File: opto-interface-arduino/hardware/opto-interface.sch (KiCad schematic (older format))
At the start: 24 parts, among them P1 CONN_02X06, P2 CONN_01X06, U1 max889, U2 LM7805, U3 LM7905

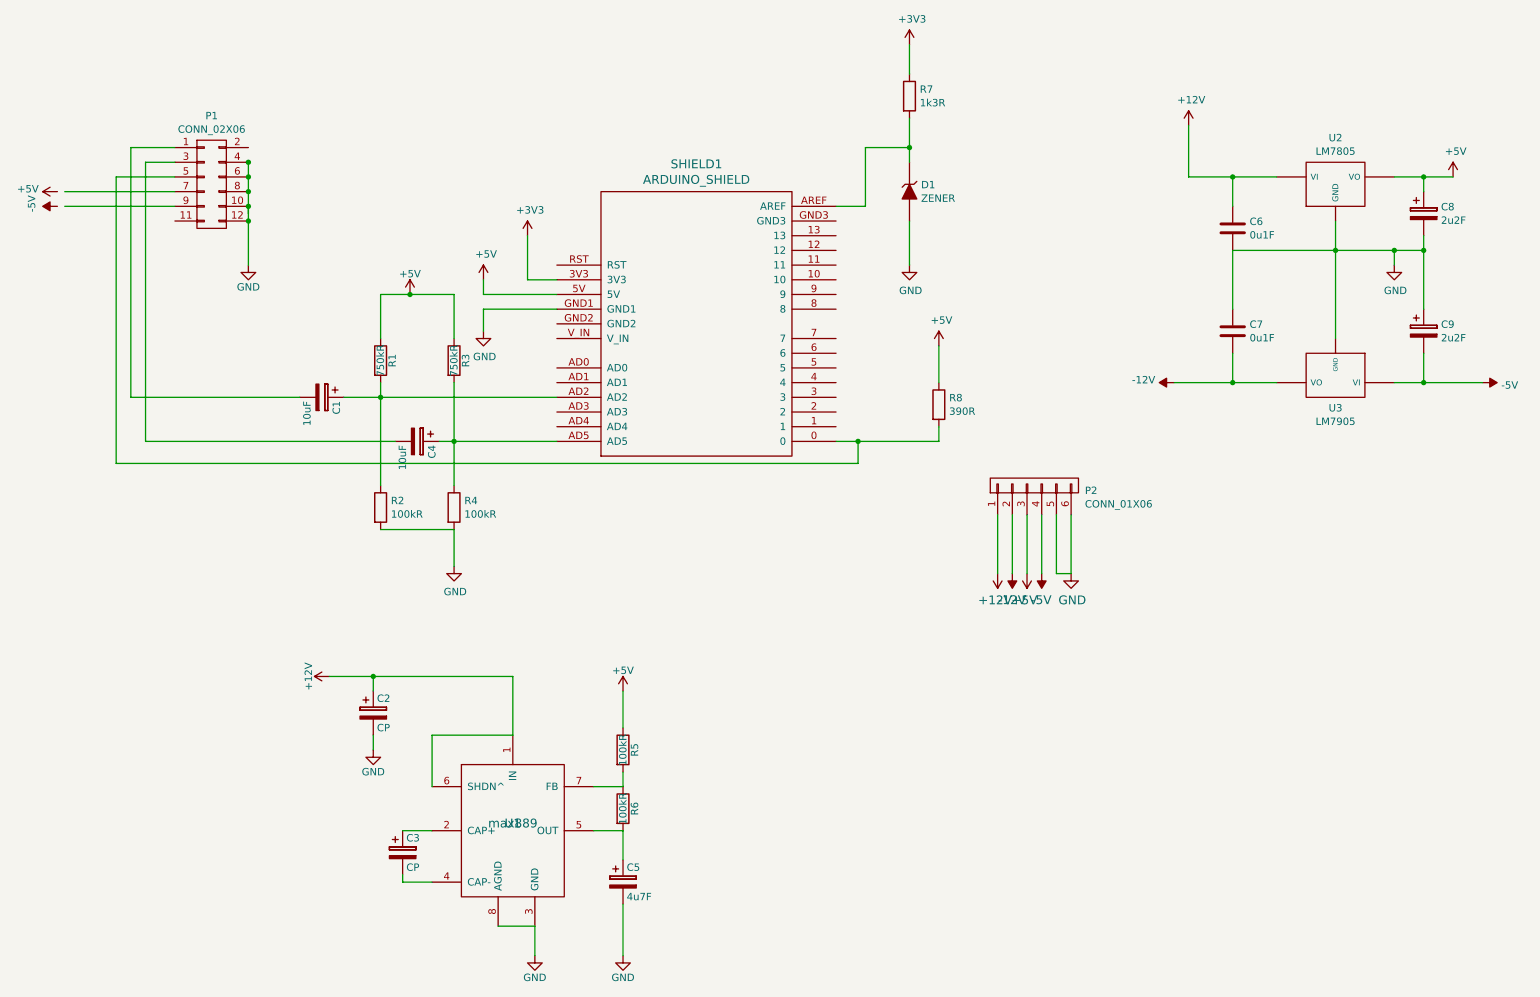
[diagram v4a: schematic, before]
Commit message: Modify layout to ahem follow the datasheet guidance on MAX889. Update analogue input schematic for simulation to accomodate steeper low-pass roll-off.
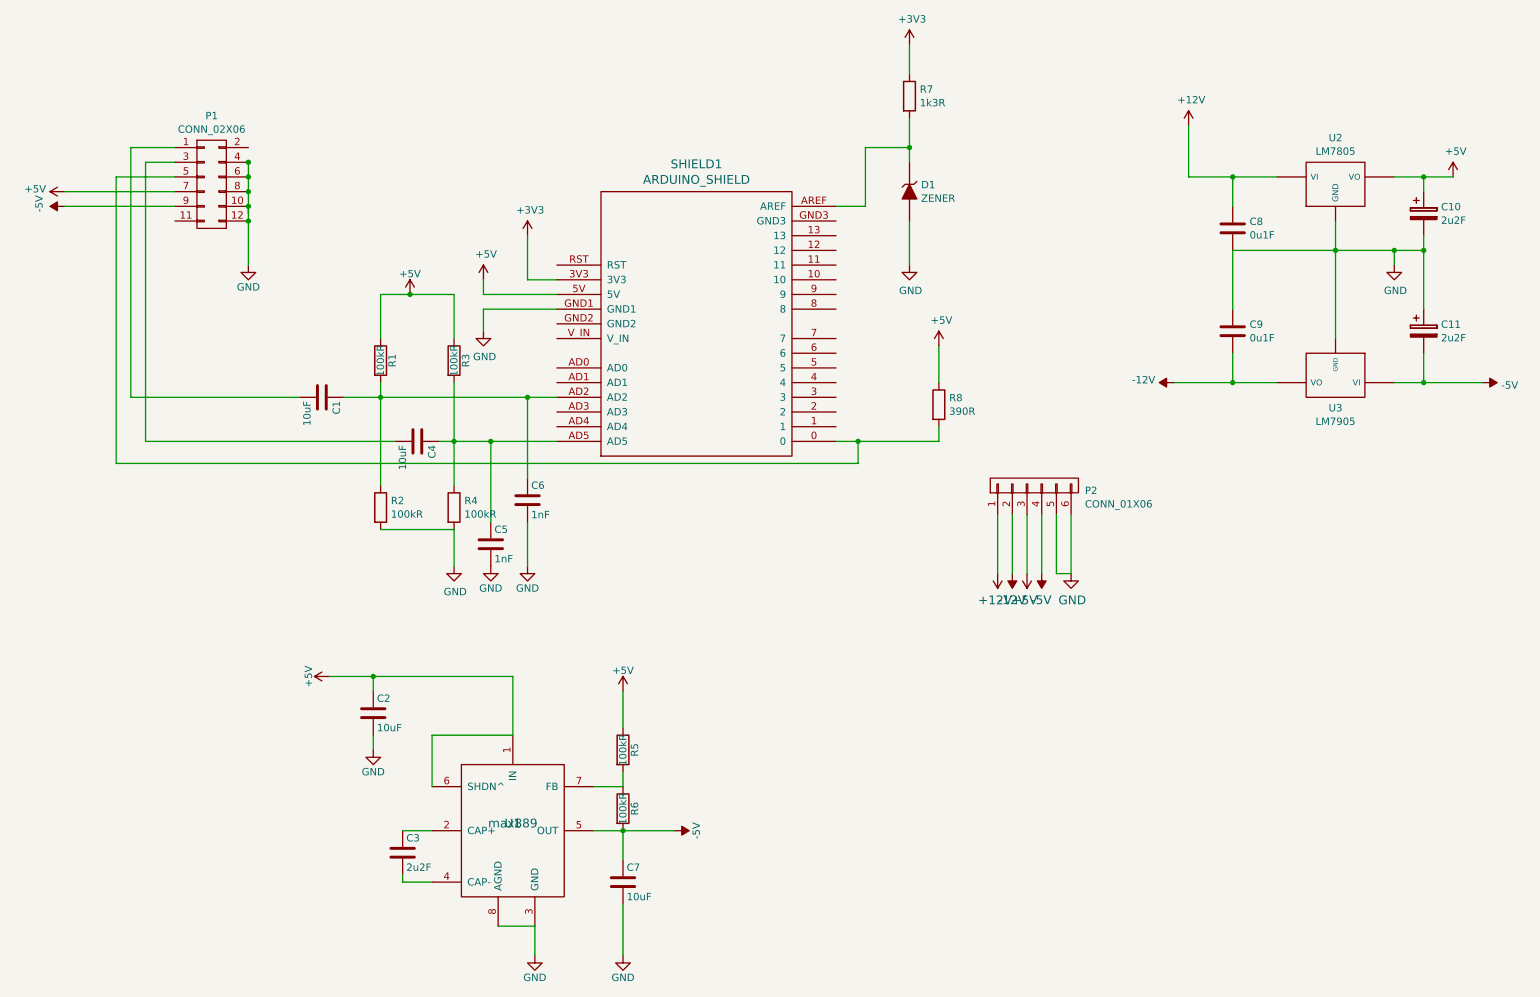
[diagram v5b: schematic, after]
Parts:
- removed C1, C4: 10uF, Discret:CP4, symbol CP
- removed C2, C3: CP, Capacitors_SMD:c_elec_8x5.4, symbol CP
- removed C5: 4u7F, Capacitors_SMD:c_elec_8x5.4, symbol CP
- added C1, C2, C4, C7: 10uF, Capacitors_SMD:C_0805_HandSoldering, symbol C
- added C3: 2u2F, Capacitors_SMD:C_0805_HandSoldering, symbol C
- added C5, C6: 1nF, Capacitors_SMD:C_0805_HandSoldering, symbol C
- R1, R3: value 750kR -> 100kR
- renumbered C8 to C10, C9 to C11, C6 to C8, C7 to C9
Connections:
- wire segments 76 -> 79
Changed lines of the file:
@@
 L -5V #PWR2
 U 1 1 56A61CAF
-P 600 1800
-F 0 "#PWR2" H 600 1900 50  0001 C CNN
-F 1 "-5V" H 618 1974 50  0000 C CNN
-F 2 "" H 600 1800 50  0000 C CNN
-F 3 "" H 600 1800 50  0000 C CNN
-	1    600  1800
+P 650 1800
+F 0 "#PWR2" H 650 1900 50  0001 C CNN
+F 1 "-5V" H 668 1974 50  0000 C CNN
+F 2 "" H 650 1800 50  0000 C CNN
+F 3 "" H 650 1800 50  0000 C CNN
+	1    650  1800
 	0    -1   -1   0
 $EndComp
@@
 L +5V #PWR03
 U 1 1 56A6320E
-P 600 1700
-F 0 "#PWR03" H 600 1550 50  0001 C CNN
-F 1 "+5V" V 618 1827 50  0000 L CNN
-F 2 "" H 600 1700 50  0000 C CNN
-F 3 "" H 600 1700 50  0000 C CNN
-	1    600  1700
+P 650 1700
+F 0 "#PWR03" H 650 1550 50  0001 C CNN
+F 1 "+5V" V 668 1827 50  0000 L CNN
+F 2 "" H 650 1700 50  0000 C CNN
+F 3 "" H 650 1700 50  0000 C CNN
+	1    650  1700
 	0    -1   -1   0
 $EndComp
@@
 	9700 1600 10100 1600
 $Comp
-L C-RESCUE-opto-interface C6
+L C-RESCUE-opto-interface C8
 U 1 1 56A63A9E
 P 8600 1950
-F 0 "C6" H 8715 1996 50  0000 L CNN
+F 0 "C8" H 8715 1996 50  0000 L CNN
 F 1 "0u1F" H 8715 1904 50  0000 L CNN
 F 2 "Capacitors_ThroughHole:C_Disc_D6_P5" H 8638 1800 50  0001 C CNN
@@
 Connection ~ 9300 2100
 $Comp
-L CP-RESCUE-opto-interface C8
+L CP-RESCUE-opto-interface C10
 U 1 1 56A63B52
 P 9900 1850
-F 0 "C8" H 10018 1896 50  0000 L CNN
+F 0 "C10" H 10018 1896 50  0000 L CNN
 F 1 "2u2F" H 10018 1804 50  0000 L CNN
 F 2 "Discret:CP5" H 9938 1700 50  0001 C CNN
@@
 $EndComp
 $Comp
-L C-RESCUE-opto-interface C7
+L C-RESCUE-opto-interface C9
 U 1 1 56A63DBB
 P 8600 2650
-F 0 "C7" H 8715 2696 50  0000 L CNN
+F 0 "C9" H 8715 2696 50  0000 L CNN
 F 1 "0u1F" H 8715 2604 50  0000 L CNN
 F 2 "Capacitors_ThroughHole:C_Disc_D6_P5" H 8638 2500 50  0001 C CNN
@@
 $EndComp
 $Comp
-L CP-RESCUE-opto-interface C9
+L CP-RESCUE-opto-interface C11
 U 1 1 56A63E65
 P 9900 2650
-F 0 "C9" H 10018 2696 50  0000 L CNN
+F 0 "C11" H 10018 2696 50  0000 L CNN
 F 1 "2u2F" H 10018 2604 50  0000 L CNN
 F 2 "Discret:CP5" H 9938 2500 50  0001 C CNN
@@
 $EndComp
 $Comp
-L -12V #PWR22
+L -12V #PWR25
 U 1 1 56A63F07
 P 8200 3000
-F 0 "#PWR22" H 8200 3100 50  0001 C CNN
+F 0 "#PWR25" H 8200 3100 50  0001 C CNN
 F 1 "-12V" V 8218 3127 50  0000 L CNN
 F 2 "" H 8200 3000 50  0000 C CNN
@@
 Connection ~ 9900 2100
 $Comp
-L -5V #PWR26
+L -5V #PWR29
 U 1 1 56A640D9
 P 10300 3000
-F 0 "#PWR26" H 10300 3100 50  0001 C CNN
+F 0 "#PWR29" H 10300 3100 50  0001 C CNN
 F 1 "-5V" V 10318 3128 50  0000 L CNN
 F 2 "" H 10300 3000 50  0000 C CNN
@@
 $EndComp
 Wire Wire Line
-	6400 1500 6400 1200
+	6400 1200 6400 1500
 Wire Wire Line
 	6400 2200 6400 1900
@@
 $EndComp
 $Comp
-L -12V #PWR18
+L -12V #PWR21
 U 1 1 56B5E808
 P 7100 4300
-F 0 "#PWR18" H 7100 4400 20  0001 C CNN
+F 0 "#PWR21" H 7100 4400 20  0001 C CNN
 F 1 "-12V" H 7102 4480 60  0000 C CNN
 F 2 "" H 7100 4300 60  0000 C CNN
@@
 $EndComp
 $Comp
-L -5V #PWR20
+L -5V #PWR23
 U 1 1 56B5E862
 P 7300 4300
-F 0 "#PWR20" H 7300 4400 20  0001 C CNN
+F 0 "#PWR23" H 7300 4400 20  0001 C CNN
 F 1 "-5V" H 7302 4480 60  0000 C CNN
 F 2 "" H 7300 4300 60  0000 C CNN
@@
 $EndComp
 $Comp
-L +12V #PWR015
-U 1 1 56D96E3B
-P 2450 5000
-F 0 "#PWR015" H 2450 4850 50  0001 C CNN
-F 1 "+12V" H 2450 5140 50  0000 C CNN
-F 2 "" H 2450 5000 50  0000 C CNN
-F 3 "" H 2450 5000 50  0000 C CNN
-	1    2450 5000
-	0    -1   -1   0
-$EndComp
-$Comp
-L CP C2
-U 1 1 56D96E9A
-P 2750 5250
-F 0 "C2" H 2775 5350 50  0000 L CNN
-F 1 "CP" H 2775 5150 50  0000 L CNN
-F 2 "Capacitors_SMD:c_elec_8x5.4" H 2788 5100 50  0001 C CNN
-F 3 "" H 2750 5250 50  0000 C CNN
-	1    2750 5250
-	1    0    0    -1
-$EndComp
-$Comp
-L GND #PWR016
+L GND #PWR015
 U 1 1 56D96EFB
 P 2750 5500
-F 0 "#PWR016" H 2750 5250 50  0001 C CNN
+F 0 "#PWR015" H 2750 5250 50  0001 C CNN
 F 1 "GND" H 2750 5350 50  0000 C CNN
 F 2 "" H 2750 5500 50  0000 C CNN
@@
 $EndComp
 $Comp
-L GND #PWR017
+L GND #PWR016
 U 1 1 56D97092
 P 3850 6900
-F 0 "#PWR017" H 3850 6650 50  0001 C CNN
+F 0 "#PWR016" H 3850 6650 50  0001 C CNN
 F 1 "GND" H 3850 6750 50  0000 C CNN
 F 2 "" H 3850 6900 50  0000 C CNN
@@
 Wire Wire Line
 	3850 6700 3850 6900
-$Comp
-L CP C3
-U 1 1 56D971F2
-P 2950 6200
-F 0 "C3" H 2975 6300 50  0000 L CNN
-F 1 "CP" H 2975 6100 50  0000 L CNN
-F 2 "Capacitors_SMD:c_elec_8x5.4" H 2988 6050 50  0001 C CNN
-F 3 "" H 2950 6200 50  0000 C CNN
-	1    2950 6200
-	1    0    0    -1
-$EndComp
 Wire Wire Line
 	2950 6050 3150 6050
@@
 	4250 5750 4450 5750
 Wire Wire Line
-	4250 6050 4450 6050
+	4250 6050 4800 6050
 Wire Wire Line
 	3150 5750 3150 5400
@@
 	1    0    0    -1
 $EndComp
-$Comp
-L CP C5
-U 1 1 56D974A2
-P 4450 6400
-F 0 "C5" H 4475 6500 50  0000 L CNN
-F 1 "4u7F" H 4475 6300 50  0000 L CNN
-F 2 "Capacitors_SMD:c_elec_8x5.4" H 4488 6250 50  0001 C CNN
-F 3 "" H 4450 6400 50  0000 C CNN
-	1    4450 6400
-	1    0    0    -1
-$EndComp
 Wire Wire Line
 	4450 6050 4450 6250
@@
 	4450 5750 4450 5650
 $Comp
-L GND #PWR018
+L GND #PWR017
 U 1 1 56D975F0
 P 4450 6900
-F 0 "#PWR018" H 4450 6650 50  0001 C CNN
+F 0 "#PWR017" H 4450 6650 50  0001 C CNN
 F 1 "GND" H 4450 6750 50  0000 C CNN
 F 2 "" H 4450 6900 50  0000 C CNN
@@
 	4450 6550 4450 6900
 $Comp
-L +5V #PWR019
+L +5V #PWR018
 U 1 1 56D9A3A4
 P 4450 5100
-F 0 "#PWR019" H 4450 4950 50  0001 C CNN
+F 0 "#PWR018" H 4450 4950 50  0001 C CNN
 F 1 "+5V" H 4450 5240 50  0000 C CNN
 F 2 "" H 4450 5100 50  0000 C CNN
@@
 	4450 5100 4450 5350
 $Comp
-L GND #PWR020
+L GND #PWR019
 U 1 1 56D9BC76
 P 1900 2200
-F 0 "#PWR020" H 1900 1950 50  0001 C CNN
+F 0 "#PWR019" H 1900 1950 50  0001 C CNN
 F 1 "GND" H 1900 2050 50  0000 C CNN
 F 2 "" H 1900 2200 50  0000 C CNN
@@
 P 2800 2850
 F 0 "R1" V 2880 2850 50  0000 C CNN
-F 1 "750kR" V 2800 2850 50  0000 C CNN
+F 1 "100kR" V 2800 2850 50  0000 C CNN
 F 2 "Resistors_SMD:R_0805_HandSoldering" V 2730 2850 50  0001 C CNN
 F 3 "" H 2800 2850 50  0000 C CNN
@@
 P 3300 2850
 F 0 "R3" V 3380 2850 50  0000 C CNN
-F 1 "750kR" V 3300 2850 50  0000 C CNN
+F 1 "100kR" V 3300 2850 50  0000 C CNN
 F 2 "Resistors_SMD:R_0805_HandSoldering" V 3230 2850 50  0001 C CNN
 F 3 "" H 3300 2850 50  0000 C CNN
@@
 $EndComp
 $Comp
-L +5V #PWR021
+L +5V #PWR020
 U 1 1 56D9C2D5
 P 3000 2400
-F 0 "#PWR021" H 3000 2250 50  0001 C CNN
+F 0 "#PWR020" H 3000 2250 50  0001 C CNN
 F 1 "+5V" H 3000 2540 50  0000 C CNN
 F 2 "" H 3000 2400 50  0000 C CNN
@@
 	3300 2400 3300 2700
 Connection ~ 3000 2400
-$Comp
-L CP C1
-U 1 1 56D9C415
+Wire Wire Line
+	2550 3100 4000 3100
+Connection ~ 2800 3100
+Wire Wire Line
+	1100 1400 1100 3100
+Wire Wire Line
+	1100 3100 2250 3100
+Wire Wire Line
+	3200 3400 4000 3400
+Wire Wire Line
+	1200 3400 2900 3400
+$Comp
+L +5V #PWR021
+U 1 1 577E7FEB
+P 2450 5000
+F 0 "#PWR021" H 2450 4850 50  0001 C CNN
+F 1 "+5V" H 2450 5140 50  0000 C CNN
+F 2 "" H 2450 5000 50  0000 C CNN
+F 3 "" H 2450 5000 50  0000 C CNN
+	1    2450 5000
+	0    -1   -1   0
+$EndComp
+$Comp
+L C C1
+U 1 1 578F4A70
 P 2400 3100
 F 0 "C1" H 2425 3200 50  0000 L CNN
 F 1 "10uF" H 2425 3000 50  0000 L CNN
-F 2 "Discret:CP4" H 2438 2950 50  0001 C CNN
+F 2 "Capacitors_SMD:C_0805_HandSoldering" H 2438 2950 50  0001 C CNN
 F 3 "" H 2400 3100 50  0000 C CNN
 	1    2400 3100
@@
 $EndComp
 $Comp
-L CP C4
-U 1 1 56D9C4C2
+L C C4
+U 1 1 578F4AD5
 P 3050 3400
 F 0 "C4" H 3075 3500 50  0000 L CNN
 F 1 "10uF" H 3075 3300 50  0000 L CNN
-F 2 "Discret:CP4" H 3088 3250 50  0001 C CNN
+F 2 "Capacitors_SMD:C_0805_HandSoldering" H 3088 3250 50  0001 C CNN
 F 3 "" H 3050 3400 50  0000 C CNN
 	1    3050 3400
 	0    1    1    0
 $EndComp
-Wire Wire Line
-	2550 3100 4000 3100
-Connection ~ 2800 3100
-Wire Wire Line
-	1100 1400 1100 3100
-Wire Wire Line
-	1100 3100 2250 3100
-Wire Wire Line
-	3200 3400 4000 3400
-Wire Wire Line
-	1200 3400 2900 3400
+$Comp
+L -5V #PWR16
+U 1 1 578F5034
+P 4800 6050
+F 0 "#PWR16" H 4800 6150 50  0001 C CNN
+F 1 "-5V" H 4800 6200 50  0000 C CNN
+F 2 "" H 4800 6050 50  0000 C CNN
+F 3 "" H 4800 6050 50  0000 C CNN
+	1    4800 6050
+	0    1    1    0
+$EndComp
+Connection ~ 4450 6050
+$Comp
+L C C2
+U 1 1 578F54FC
+P 2750 5250
+F 0 "C2" H 2775 5350 50  0000 L CNN
+F 1 "10uF" H 2775 5150 50  0000 L CNN
+F 2 "Capacitors_SMD:C_0805_HandSoldering" H 2788 5100 50  0001 C CNN
+F 3 "" H 2750 5250 50  0000 C CNN
+	1    2750 5250
+	1    0    0    -1
+$EndComp
+$Comp
+L C C3
+U 1 1 578F564E
+P 2950 6200
+F 0 "C3" H 2975 6300 50  0000 L CNN
+F 1 "2u2F" H 2975 6100 50  0000 L CNN
+F 2 "Capacitors_SMD:C_0805_HandSoldering" H 2988 6050 50  0001 C CNN
+F 3 "" H 2950 6200 50  0000 C CNN
+	1    2950 6200
+	1    0    0    -1
+$EndComp
+$Comp
+L C C7
+U 1 1 578F588B
+P 4450 6400
+F 0 "C7" H 4475 6500 50  0000 L CNN
+F 1 "10uF" H 4475 6300 50  0000 L CNN
+F 2 "Capacitors_SMD:C_0805_HandSoldering" H 4488 6250 50  0001 C CNN
+F 3 "" H 4450 6400 50  0000 C CNN
+	1    4450 6400
+	1    0    0    -1
+$EndComp
+$Comp
+L C C5
+U 1 1 578F5FAA
+P 3550 4100
+F 0 "C5" H 3575 4200 50  0000 L CNN
+F 1 "1nF" H 3575 4000 50  0000 L CNN
+F 2 "Capacitors_SMD:C_0805_HandSoldering" H 3588 3950 50  0001 C CNN
+F 3 "" H 3550 4100 50  0000 C CNN
+	1    3550 4100
+	1    0    0    -1
+$EndComp
+$Comp
+L C C6
+U 1 1 578F60E3
+P 3800 3800
+F 0 "C6" H 3825 3900 50  0000 L CNN
+F 1 "1nF" H 3825 3700 50  0000 L CNN
+F 2 "Capacitors_SMD:C_0805_HandSoldering" H 3838 3650 50  0001 C CNN
+F 3 "" H 3800 3800 50  0000 C CNN
+	1    3800 3800
+	1    0    0    -1
+$EndComp
+Wire Wire Line
+	3800 3650 3800 3100
+Connection ~ 3800 3100
+Wire Wire Line
+	3550 3950 3550 3400
+Connection ~ 3550 3400
+$Comp
+L GND #PWR022
+U 1 1 578F6339
+P 3550 4250
+F 0 "#PWR022" H 3550 4000 50  0001 C CNN
+F 1 "GND" H 3550 4100 50  0000 C CNN
+F 2 "" H 3550 4250 50  0000 C CNN
+F 3 "" H 3550 4250 50  0000 C CNN
+	1    3550 4250
+	1    0    0    -1
+$EndComp
+$Comp
+L GND #PWR023
+U 1 1 578F6381
+P 3800 4250
+F 0 "#PWR023" H 3800 4000 50  0001 C CNN
+F 1 "GND" H 3800 4100 50  0000 C CNN
+F 2 "" H 3800 4250 50  0000 C CNN
+F 3 "" H 3800 4250 50  0000 C CNN
+	1    3800 4250
+	1    0    0    -1
+$EndComp
+Wire Wire Line
+	3800 3950 3800 4250
 $EndSCHEMATC
